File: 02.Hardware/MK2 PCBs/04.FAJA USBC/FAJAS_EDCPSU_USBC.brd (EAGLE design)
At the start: 42.8 x 41.6 mm, 28 parts, among them K1 FLEX_DCDC, K2 FLEX_DCDC, K3 FLEX_CONN, K4 FLEX8, K5 FLEX8

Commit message: Flex MK2 Creation
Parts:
- removed DISP_CPU_1, DISP_CPU_4: DISP_CPU_1, Flex_Faja_connector:FLEX6
- removed DISP_CPU_2, DISP_CPU_3: DISP_CPU_2, Flex_Faja_connector:FLEX6
- removed FLX1, FLX10, FLX11, FLX2, FLX3, FLX4, FLX5, FLX6, FLX7, FLX8, FLX9: FLEX4, Flex4:FLEX4
- removed GND1, GND2, VO+, VO+1, VO-, VO-1, VSYS_IP, VSYS_IP1: TESTPAD_TPSQTP15SQ, BeagleBone_Blue_R3:TESTPAD_TP15SQ
- removed K3: FLEX_CONN, Flex4:FLEX4
- K1, K2: value FLEX_DCDC -> FLEX_MK2
- K4, K5: value FLEX8 -> FLEX_MK2
- moved K4 29.5 mm to (38.6, 24.1)
- moved K5 29.5 mm to (38.1, 24.1)
- moved K1 22.3 mm to (34.6, 41.7), turned to 180 degrees
- moved K2 22.0 mm to (34.6, 41.2), turned to 0 degrees
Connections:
- net CPU-DCDC_1 renamed P-
- net CPU-DCDC_2 renamed P+
- net CPU-DCDC_3 renamed SEL
- net CPU-DCDC_4 renamed VCC
- removed net BUTTON-INPUT_1: FLX1.1, FLX6.1, FLX8.1, FLX9.1
- removed net BUTTON-INPUT_2: FLX1.2, FLX6.2, FLX8.2, FLX9.2
- removed net BUTTON-INPUT_3: FLX1.3, FLX6.3, FLX8.3, FLX9.3
- removed net BUTTON-INPUT_4: FLX1.4, FLX6.4, FLX8.4, FLX9.4
- removed net CPU-CONN_1: FLX10.1, FLX11.1, FLX3.1, K3.1
- removed net CPU-CONN_2: FLX10.2, FLX11.2, FLX3.2, K3.2
- removed net CPU-CONN_3: FLX10.3, FLX11.3, FLX3.3, K3.3
- removed net CPU-CONN_4: FLX10.4, FLX11.4, FLX3.4, K3.4
- removed net CPU-DCDC_5: K1.5, K2.5, K4.5, K5.5
- removed net CPU-DCDC_6: K1.6, K2.6, K4.6, K5.6
- removed net CPU-DCDC_7: K1.7, K2.7, K4.7, K5.7
- removed net CPU-DCDC_8: K1.8, K2.8, K4.8, K5.8
- removed net DSP-CPU_1: DISP_CPU_1.1, DISP_CPU_2.1, DISP_CPU_3.1, DISP_CPU_4.1
- removed net DSP-CPU_2: DISP_CPU_1.2, DISP_CPU_2.2, DISP_CPU_3.2, DISP_CPU_4.2
- removed net DSP-CPU_3: DISP_CPU_1.3, DISP_CPU_2.3, DISP_CPU_3.3, DISP_CPU_4.3
- removed net DSP-CPU_4: DISP_CPU_1.4, DISP_CPU_2.4, DISP_CPU_3.4, DISP_CPU_4.4
- removed net DSP-CPU_5: DISP_CPU_1.5, DISP_CPU_2.5, DISP_CPU_3.5, DISP_CPU_4.5
- removed net DSP-CPU_6: DISP_CPU_1.6, DISP_CPU_2.6, DISP_CPU_3.6, DISP_CPU_4.6
- removed net VOUT+: FLX2.1, FLX2.2, FLX4.1, FLX4.2, VO+.TP, VO+1.TP
- removed net VOUT-: FLX2.3, FLX2.4, FLX4.3, FLX4.4, VO-.TP, VO-1.TP
- removed net VSYS: FLX5.3, FLX5.4, FLX7.3, FLX7.4, VSYS_IP.TP, VSYS_IP1.TP
- new net VOUT: K1.5, K1.6, K2.5, K2.6, K4.5, K4.6, K5.5, K5.6
- net GND: now also K1.7, K1.8, K2.7, K2.8, K4.7, K4.8, K5.7, K5.8; no longer FLX5.1, FLX5.2, FLX7.1, FLX7.2, GND1.TP, GND2.TP
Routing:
- net VOUT+: track 84.8 -> 0.00 mm, vias 10 -> 0
- net VOUT-: track 84.7 -> 0.00 mm, vias 10 -> 0
- net CPU-DCDC_5: track 82.6 -> 0.00 mm, vias 6 -> 0
- net BUTTON-INPUT_4: track 81.4 -> 0.00 mm, vias 6 -> 0
- net BUTTON-INPUT_2: track 81.1 -> 0.00 mm, vias 6 -> 0
- net BUTTON-INPUT_3: track 81.1 -> 0.00 mm, vias 6 -> 0
- net BUTTON-INPUT_1: track 81.1 -> 0.00 mm, vias 6 -> 0
- net CPU-DCDC_7: track 80.7 -> 0.00 mm, vias 6 -> 0
- net CPU-DCDC_6: track 80.7 -> 0.00 mm, vias 6 -> 0
- net CPU-DCDC_8: track 80.3 -> 0.00 mm, vias 6 -> 0
- net DSP-CPU_4: track 70.0 -> 0.00 mm, vias 6 -> 0
- net DSP-CPU_6: track 69.4 -> 0.00 mm, vias 6 -> 0
- net DSP-CPU_2: track 69.4 -> 0.00 mm, vias 6 -> 0
- net DSP-CPU_5: track 68.3 -> 0.00 mm, vias 6 -> 0
- net DSP-CPU_3: track 68.0 -> 0.00 mm, vias 6 -> 0
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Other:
- board size 42.8 x 41.6 mm -> 8.9 x 22.5 mm
- board text added: "v1-Jun22"
- board text removed: "CONNECTOR - DCDC Jun-21 v2"
- board text removed: "CPU - CONNECTOR Jun-21 v2"
- board text removed: "CPU - DCDC Jun-21 v2"
- board text removed: "CPU - DISP Jun-21 v2"
- board text removed: "INPUT - BUTTON Jun-21 v2"

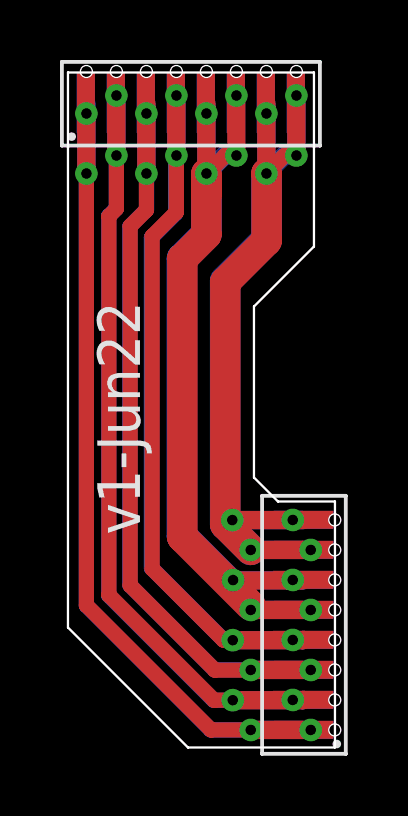
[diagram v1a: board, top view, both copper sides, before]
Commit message: Cleanup trazado + GERBERs
Versión de primera compra a PCBWAY
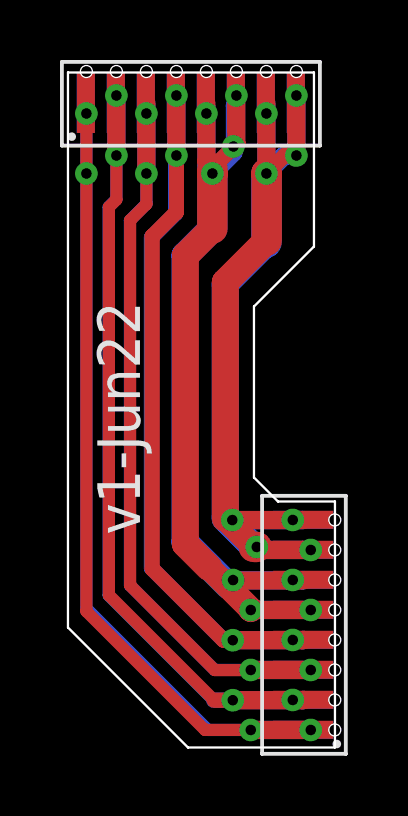
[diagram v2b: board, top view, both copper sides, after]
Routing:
- net VOUT: track 54.1 -> 52.3 mm

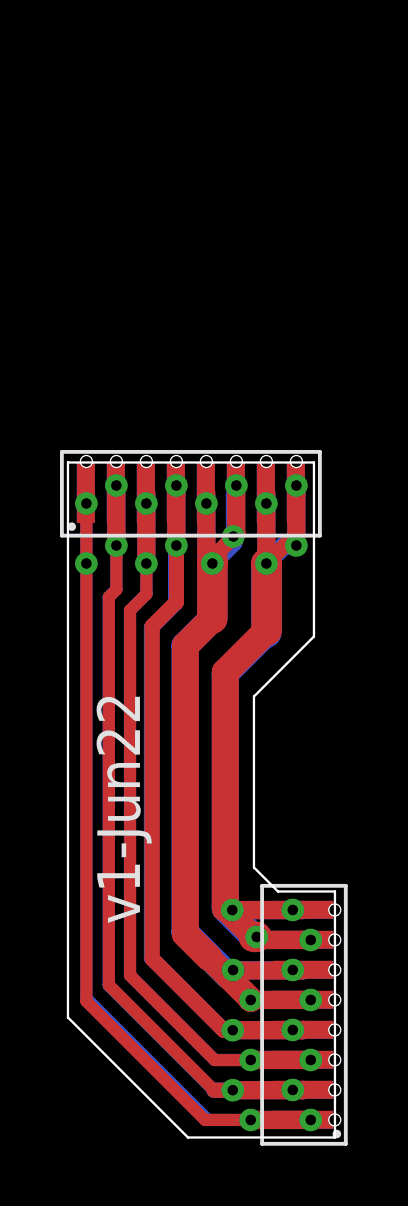
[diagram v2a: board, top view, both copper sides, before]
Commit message: Cambio dimension Fajas. Cierre Issue #9
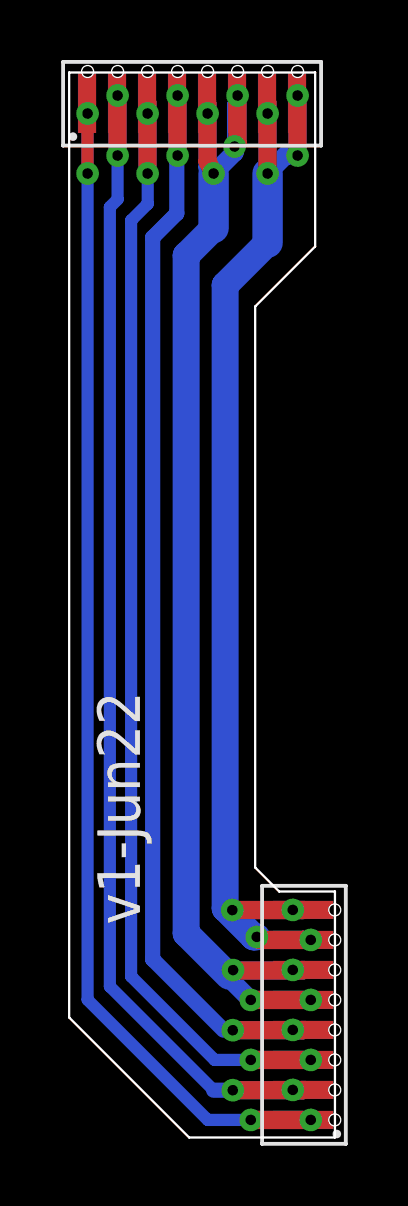
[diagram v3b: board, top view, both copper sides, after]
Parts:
- moved K1 13.0 mm to (34.6, 54.7)
- moved K2 13.0 mm to (34.6, 54.2)
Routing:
- net P-: track 51.2 -> 42.5 mm
- net P+: track 49.2 -> 41.8 mm
- net SEL: track 46.8 -> 40.6 mm
- net VOUT: track 52.3 -> 47.0 mm
- net VCC: track 43.8 -> 39.0 mm
- net GND: track 46.0 -> 44.3 mm
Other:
- board size 8.9 x 22.5 mm -> 8.9 x 35.5 mm
